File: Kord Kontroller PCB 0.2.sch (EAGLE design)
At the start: 190 parts, among them IC2 74HCT1G125DBV, IC4 ATSAMD51G_TQFN48, J1 MIDIOUTB, J2 MIDIOUTA, SW1 SPST_TACT-KMR2, U1 AP2112K-3.3, U2 ATSAMD51J19A-AUT, X3 microUSB

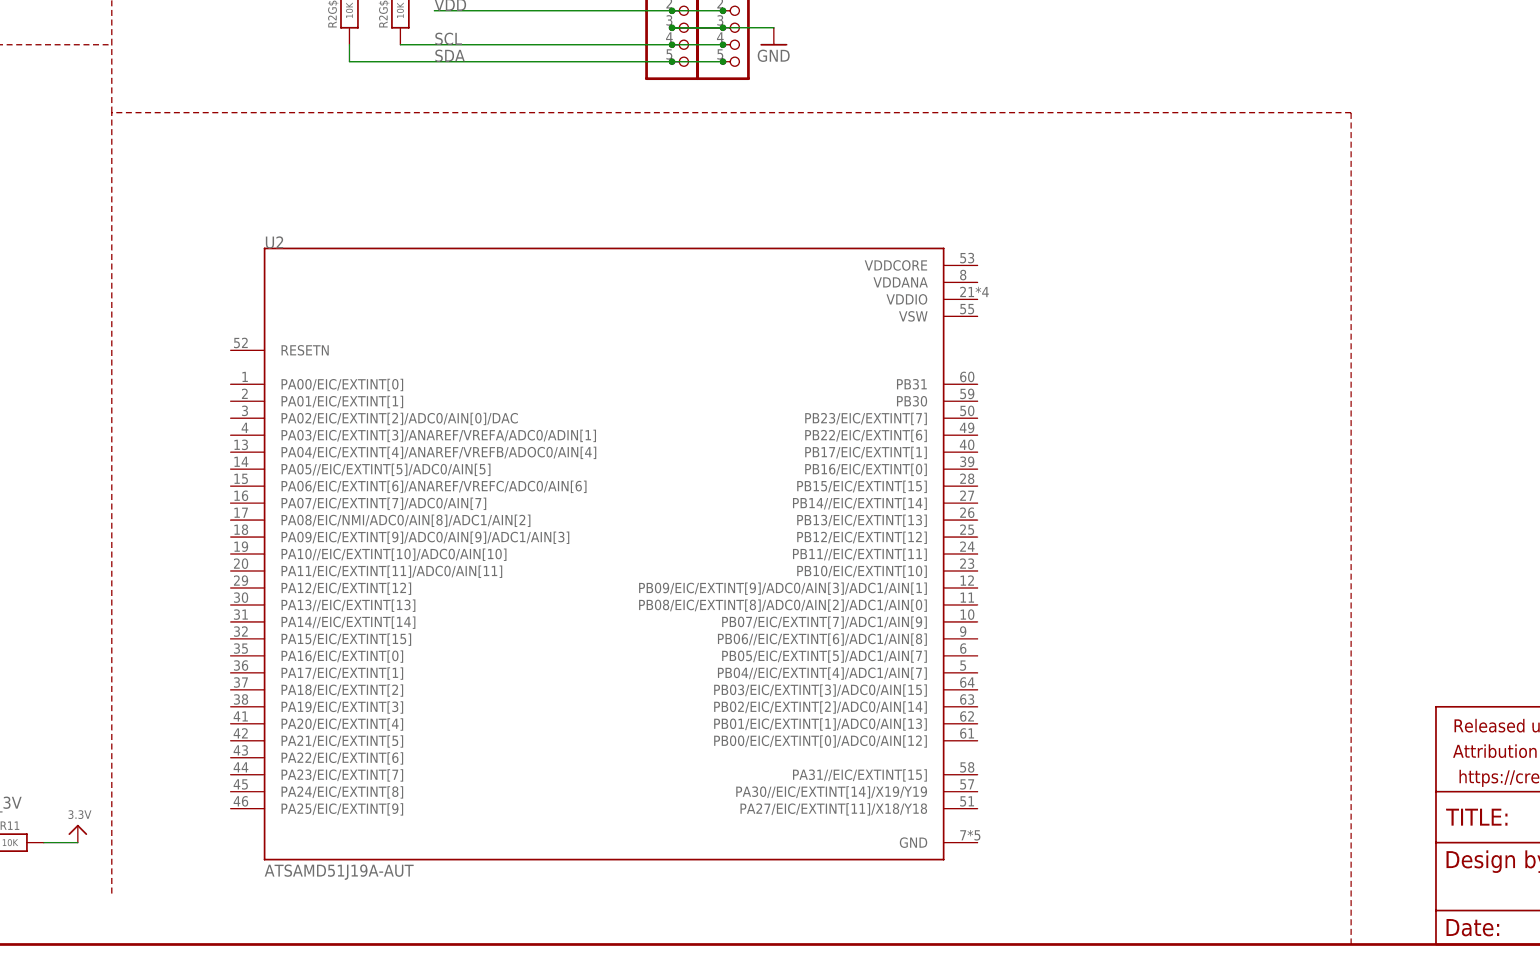
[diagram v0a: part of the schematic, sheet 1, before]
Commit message: Added lines to new 64-QFN part
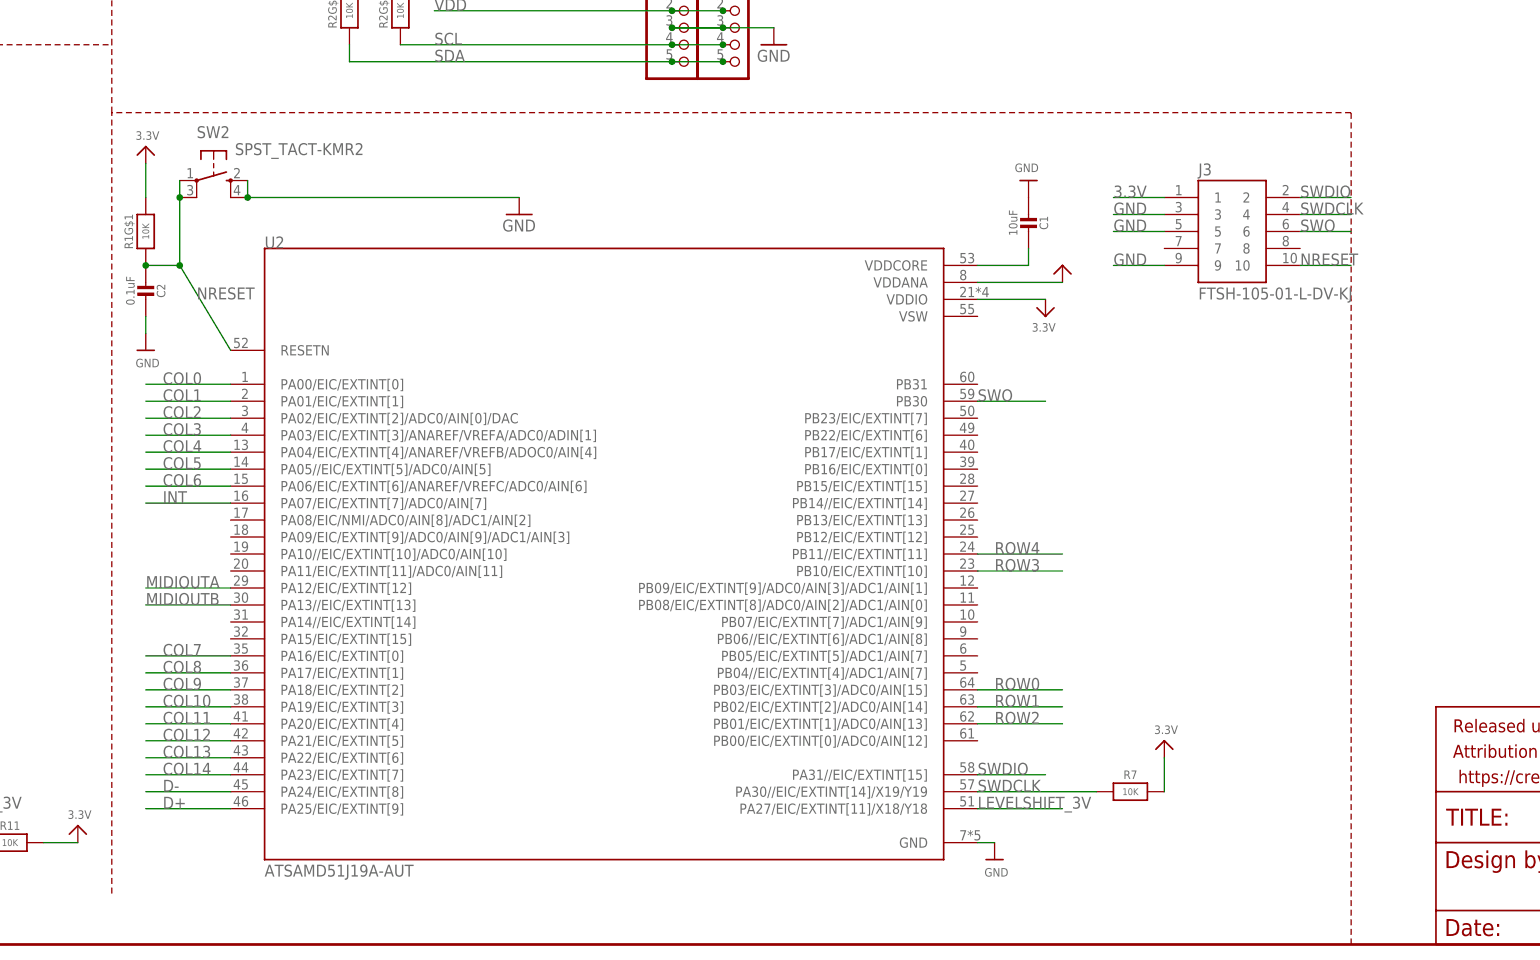
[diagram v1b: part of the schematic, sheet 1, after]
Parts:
- added C1: 10uF, microbuilder:CAP_CERAMIC0805-NOOUTLINE
- added C2: 0.1uF, microbuilder:CAP_CERAMIC0603_NO
- added J3: FTSH-105-01-L-DV-KJ, FTSH-105-01-L-DV-K:FTSH-105-01-L-DV-KJ
- added R1: 10K, microbuilder:RESISTOR_4PACK
- added R7: 10K, microbuilder:RESISTOR_0603_NOOUT
- added SW2: SPST_TACT-KMR2, adafruit:SPST_TACT-KMR2
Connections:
- new net NRESET: C2.2, J3.10, R1G$1.1, SW2.P, SW2.P1, U2.RESETN
- new net SWDCLK: J3.4, R7.1, U2.PA30//EIC/EXTINT[14]/X19/Y19
- new net SWO: J3.6, U2.PB30
- new net VDDCORE1: C1.1, U2.VDDCORE
- net 3.3V: now also J3.1, R1G$1.2, R7.2, U2.VDDIO
- net AVDD: now also U2.VDDANA
- net COL0: now also U2.PA00/EIC/EXTINT[0]
- net COL1: now also U2.PA01/EIC/EXTINT[1]
- net COL10: now also U2.PA19/EIC/EXTINT[3]
- net COL11: now also U2.PA20/EIC/EXTINT[4]
- net COL12: now also U2.PA21/EIC/EXTINT[5]
- net COL13: now also U2.PA22/EIC/EXTINT[6]
- net COL14: now also U2.PA23/EIC/EXTINT[7]
- net COL2: now also U2.PA02/EIC/EXTINT[2]/ADC0/AIN[0]/DAC
- net COL3: now also U2.PA03/EIC/EXTINT[3]/ANAREF/VREFA/ADC0/ADIN[1]
- net COL4: now also U2.PA04/EIC/EXTINT[4]/ANAREF/VREFB/ADOC0/AIN[4]
- net COL5: now also U2.PA05//EIC/EXTINT[5]/ADC0/AIN[5]
- net COL6: now also U2.PA06/EIC/EXTINT[6]/ANAREF/VREFC/ADC0/AIN[6]
- net COL7: now also U2.PA16/EIC/EXTINT[0]
- net COL8: now also U2.PA17/EIC/EXTINT[1]
- net COL9: now also U2.PA18/EIC/EXTINT[2]
- net D+: now also U2.PA25/EIC/EXTINT[9]
- net D-: now also U2.PA24/EIC/EXTINT[8]
- net GND: now also C1.2, C2.1, J3.3, J3.5, J3.9, SW2.S, SW2.S1, U2.GND
- net INT: now also U2.PA07/EIC/EXTINT[7]/ADC0/AIN[7]
- net LEVELSHIFT_3V: now also U2.PA27/EIC/EXTINT[11]/X18/Y18
- net MIDIOUTA: now also U2.PA12/EIC/EXTINT[12]
- net MIDIOUTB: now also U2.PA13//EIC/EXTINT[13]
- net ROW0: now also U2.PB03/EIC/EXTINT[3]/ADC0/AIN[15]
- net ROW1: now also U2.PB02/EIC/EXTINT[2]/ADC0/AIN[14]
- net ROW2: now also U2.PB01/EIC/EXTINT[1]/ADC0/AIN[13]
- net ROW3: now also U2.PB10/EIC/EXTINT[10]
- net ROW4: now also U2.PB11//EIC/EXTINT[11]
- net SWDIO: now also J3.2, U2.PA31//EIC/EXTINT[15]

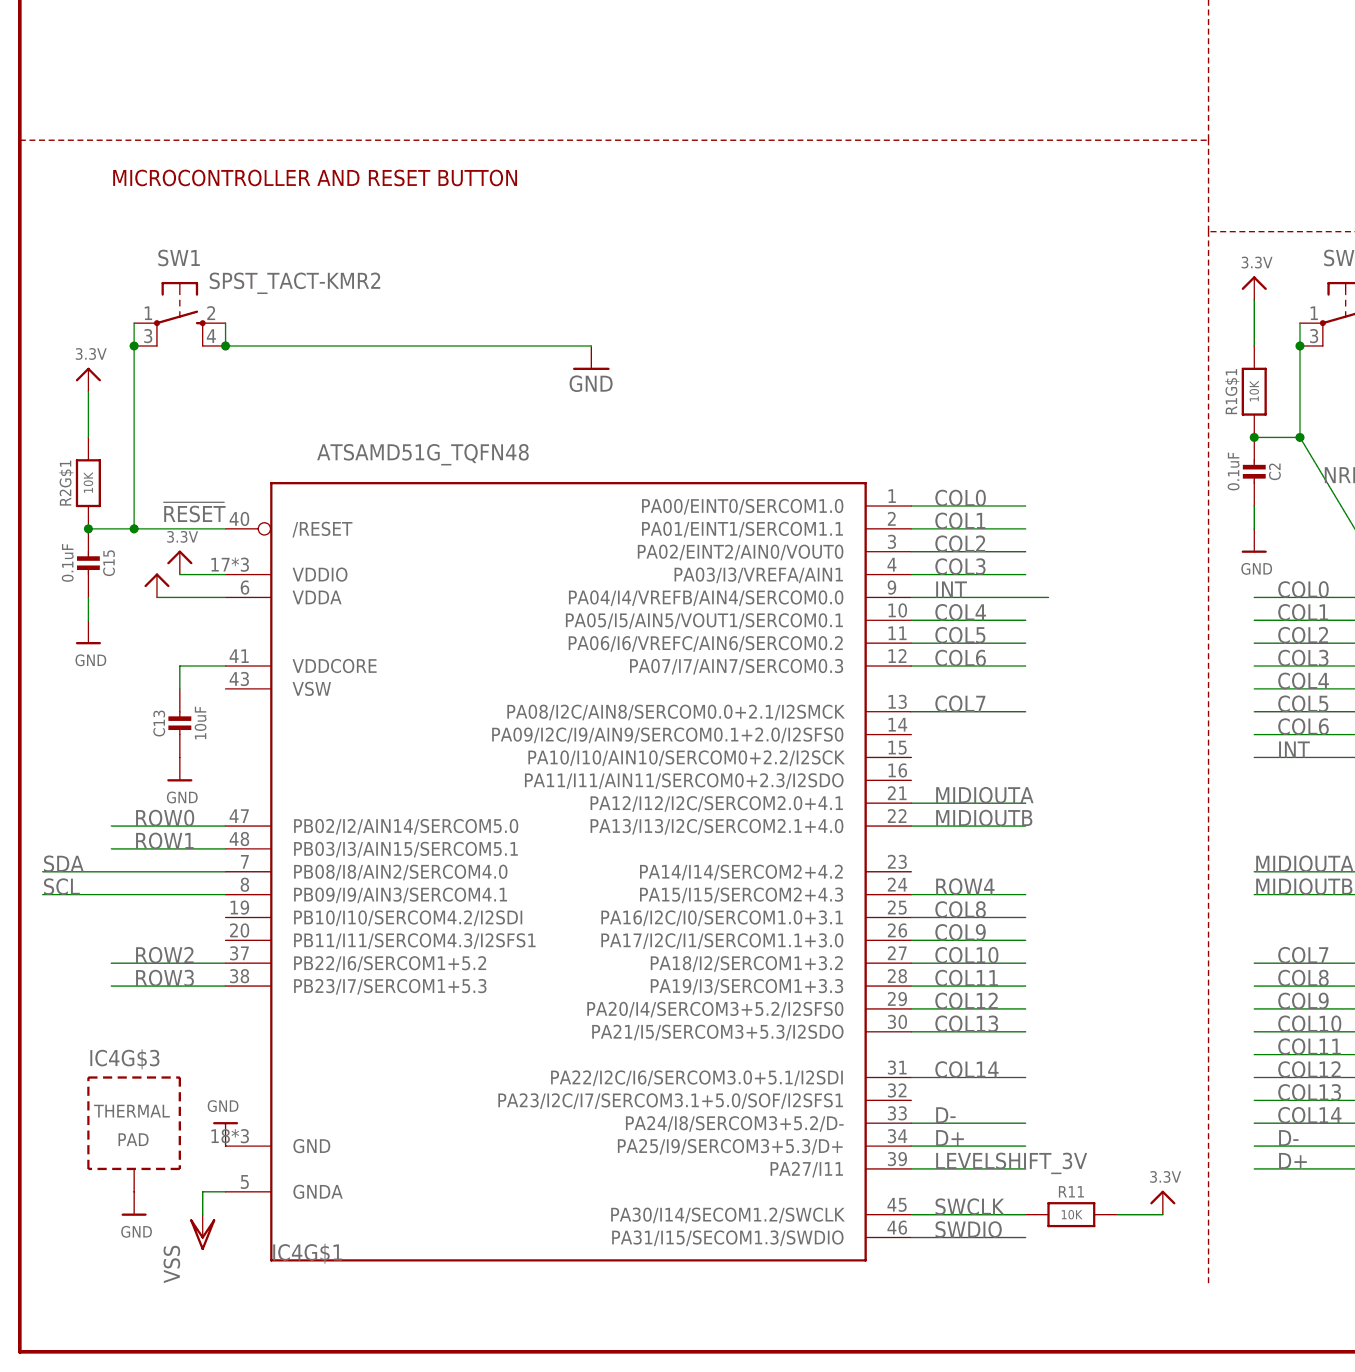
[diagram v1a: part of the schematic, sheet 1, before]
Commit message: Deleted TQFN8 pin package for 64 pin package
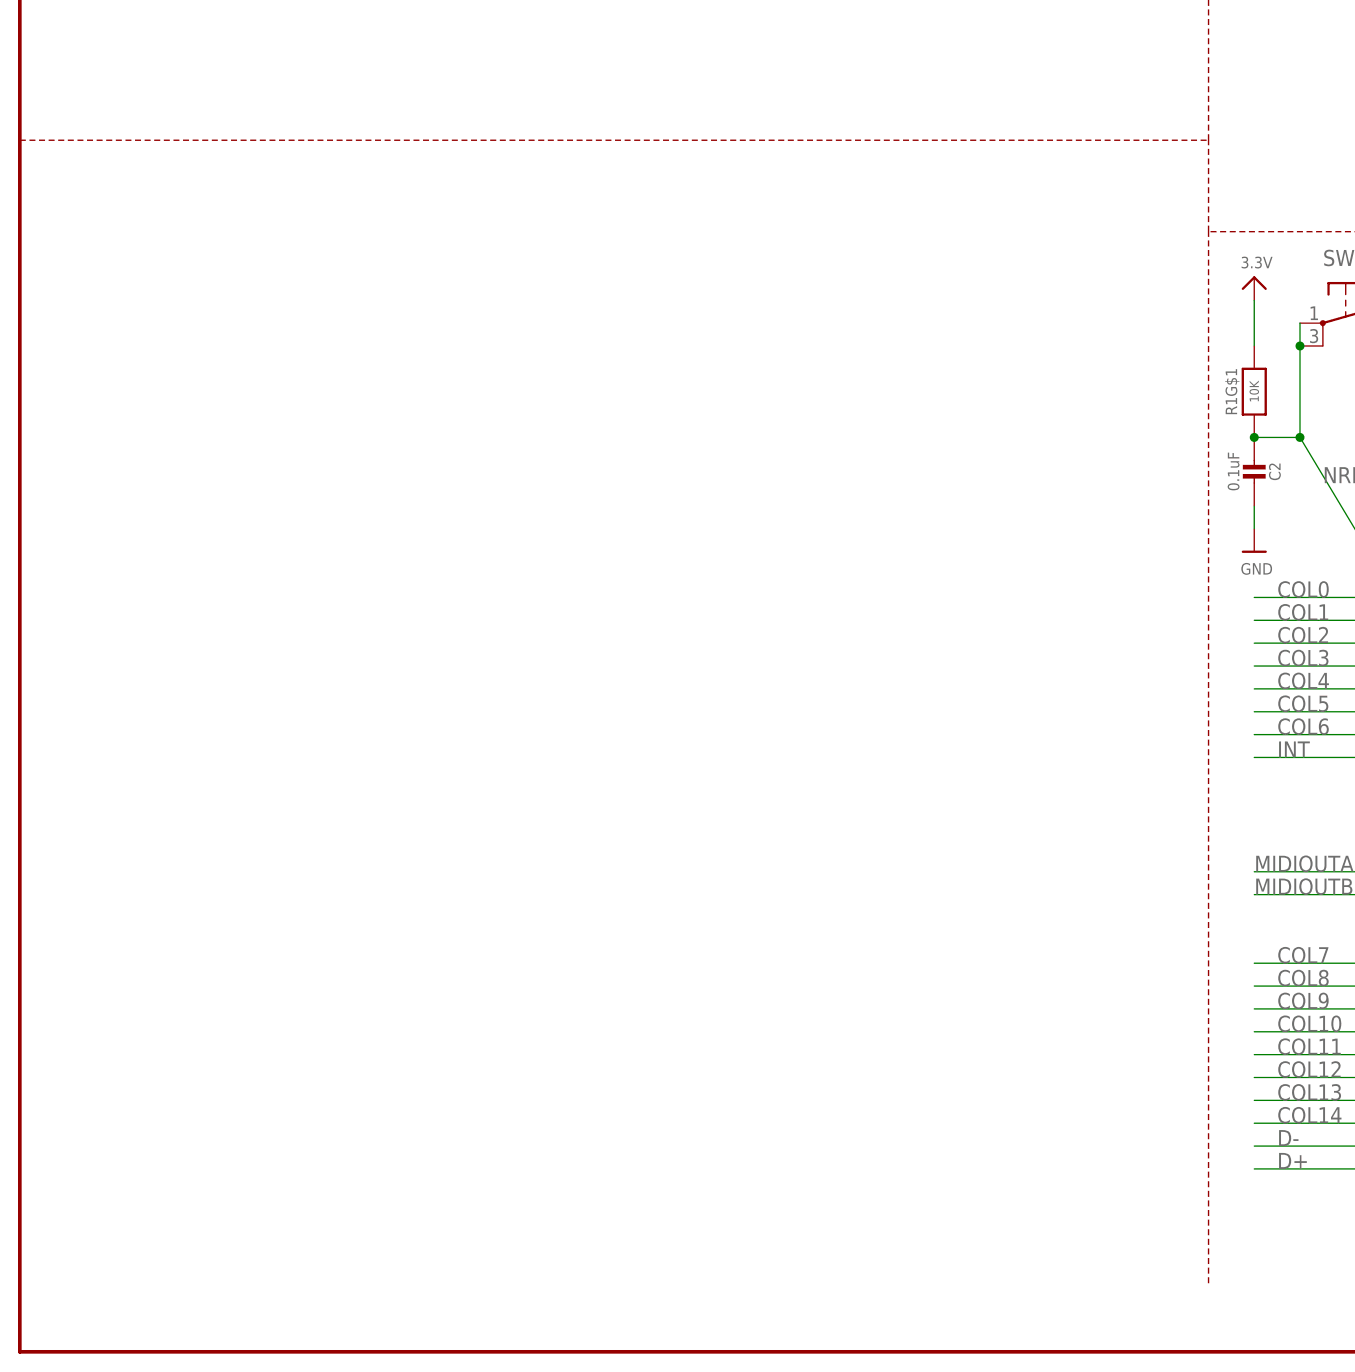
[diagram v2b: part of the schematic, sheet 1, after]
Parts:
- removed C13: 10uF, microbuilder:CAP_CERAMIC0805-NOOUTLINE
- removed C15: 0.1uF, microbuilder:CAP_CERAMIC0603_NO
- removed IC4: ATSAMD51G_TQFN48, microbuilder:ATSAMD51G_TQFN48
- removed R11: 10K, microbuilder:RESISTOR_0603_NOOUT
- removed SW1: SPST_TACT-KMR2, adafruit:SPST_TACT-KMR2
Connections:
- removed net !RESET: C15.2, IC4G$1./RESET, R2G$1.1, SW1.P, SW1.P1
- removed net SWCLK: IC4G$1.PA30/I14/SECOM1.2/SWCLK, R11.1
- removed net VDDCORE: C13.1, IC4G$1.VDDCORE
- removed net VSS: IC4G$1.GNDA
- net 3.3V: no longer IC4G$1.VDDIO, R11.2, R2G$1.2
- net AVDD: no longer IC4G$1.VDDA
- net COL0: no longer IC4G$1.PA00/EINT0/SERCOM1.0
- net COL1: no longer IC4G$1.PA01/EINT1/SERCOM1.1
- net COL10: no longer IC4G$1.PA18/I2/SERCOM1+3.2
- net COL11: no longer IC4G$1.PA19/I3/SERCOM1+3.3
- net COL12: no longer IC4G$1.PA20/I4/SERCOM3+5.2/I2SFS0
- net COL13: no longer IC4G$1.PA21/I5/SERCOM3+5.3/I2SDO
- net COL14: no longer IC4G$1.PA22/I2C/I6/SERCOM3.0+5.1/I2SDI
- net COL2: no longer IC4G$1.PA02/EINT2/AIN0/VOUT0
- net COL3: no longer IC4G$1.PA03/I3/VREFA/AIN1
- net COL4: no longer IC4G$1.PA05/I5/AIN5/VOUT1/SERCOM0.1
- net COL5: no longer IC4G$1.PA06/I6/VREFC/AIN6/SERCOM0.2
- net COL6: no longer IC4G$1.PA07/I7/AIN7/SERCOM0.3
- net COL7: no longer IC4G$1.PA08/I2C/AIN8/SERCOM0.0+2.1/I2SMCK
- net COL8: no longer IC4G$1.PA16/I2C/I0/SERCOM1.0+3.1
- net COL9: no longer IC4G$1.PA17/I2C/I1/SERCOM1.1+3.0
- net D+: no longer IC4G$1.PA25/I9/SERCOM3+5.3/D+
- net D-: no longer IC4G$1.PA24/I8/SERCOM3+5.2/D-
- net GND: no longer C13.2, C15.1, IC4G$1.GND, IC4G$3.TP, SW1.S, SW1.S1
- net INT: no longer IC4G$1.PA04/I4/VREFB/AIN4/SERCOM0.0
- net LEVELSHIFT_3V: no longer IC4G$1.PA27/I11
- net MIDIOUTA: no longer IC4G$1.PA12/I12/I2C/SERCOM2.0+4.1
- net MIDIOUTB: no longer IC4G$1.PA13/I13/I2C/SERCOM2.1+4.0
- net ROW0: no longer IC4G$1.PB02/I2/AIN14/SERCOM5.0
- net ROW1: no longer IC4G$1.PB03/I3/AIN15/SERCOM5.1
- net ROW2: no longer IC4G$1.PB22/I6/SERCOM1+5.2
- net ROW3: no longer IC4G$1.PB23/I7/SERCOM1+5.3
- net ROW4: no longer IC4G$1.PA15/I15/SERCOM2+4.3
- net SCL: no longer IC4G$1.PB09/I9/AIN3/SERCOM4.1
- net SDA: no longer IC4G$1.PB08/I8/AIN2/SERCOM4.0
- net SWDIO: no longer IC4G$1.PA31/I15/SECOM1.3/SWDIO
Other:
- note removed: "MICROCONTROLLER AND RESET BUTTON"
